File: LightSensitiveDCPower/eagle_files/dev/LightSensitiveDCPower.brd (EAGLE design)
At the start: 12 x 17.5 mm, 5 parts, among them SW1 PCM12SMTR

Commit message: Elongate board to save for wiidth. Check point.
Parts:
- moved OUT 4.47 mm to (6.00, 2.00), turned to 0 degrees
- moved PC1 4.03 mm to (6.00, 14.5)
- moved R1 4.03 mm to (5.50, 7.50)
- moved IN 3.92 mm to (5.00, 19.0)
- moved SW1 1.58 mm to (2.00, 12.5)
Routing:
- net N$1: track 21.2 -> 27.8 mm
- net N$2: track 2.68 -> 4.66 mm
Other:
- board size 12 x 17.5 mm -> 10 x 21 mm
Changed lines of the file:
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@@
 <layer number="37" name="tTest" color="7" fill="1" visible="no" active="yes"/>
 <layer number="38" name="bTest" color="7" fill="1" visible="no" active="yes"/>
-<layer number="39" name="tKeepout" color="4" fill="11" visible="no" active="yes"/>
+<layer number="39" name="tKeepout" color="4" fill="11" visible="yes" active="yes"/>
 <layer number="40" name="bKeepout" color="1" fill="11" visible="yes" active="yes"/>
 <layer number="41" name="tRestrict" color="4" fill="10" visible="yes" active="yes"/>
@@
 <board>
 <plain>
-<wire x1="0" y1="0" x2="12" y2="0" width="0" layer="20"/>
-<wire x1="12" y1="0" x2="12" y2="17.5" width="0" layer="20"/>
-<wire x1="12" y1="17.5" x2="0" y2="17.5" width="0" layer="20"/>
-<wire x1="0" y1="17.5" x2="0" y2="0" width="0" layer="20"/>
-<text x="2" y="15.25" size="0.6096" layer="51">VIN</text>
-<text x="1.25" y="0.5" size="0.6096" layer="51">VOUT</text>
-<text x="1.25" y="7" size="0.6096" layer="51">GND</text>
-<text x="10" y="15.25" size="0.6096" layer="51">GND</text>
-<text x="1.46" y="10.41" size="0.3048" layer="51">LiSePow
+<wire x1="0" y1="-0.01" x2="10" y2="0" width="0" layer="20"/>
+<wire x1="10" y1="0" x2="10" y2="21" width="0" layer="20"/>
+<wire x1="10" y1="21" x2="-0.01" y2="21" width="0" layer="20"/>
+<wire x1="-0.01" y1="21" x2="0" y2="-0.01" width="0" layer="20"/>
+<text x="0.7" y="18.5" size="0.6096" layer="51">VIN</text>
+<text x="9.49" y="0.88" size="0.6096" layer="51" rot="R90">VOUT</text>
+<text x="2.77" y="1.16" size="0.6096" layer="51" rot="R90">GND</text>
+<text x="8" y="18.5" size="0.6096" layer="51">GND</text>
+<text x="1.31" y="12.87" size="0.3048" layer="51">LiSePow
 Rev1
 09/19/14</text>
@@
 </autorouter>
 <elements>
-<element name="IN" library="pinhead" package="1X02" value="" x="6.67" y="15.45" smashed="yes" rot="R180">
-<attribute name="VALUE" x="9.21" y="18.625" size="1.27" layer="27" rot="R180"/>
-</element>
-<element name="OUT" library="pinhead" package="1X02" value="" x="2" y="4" smashed="yes" rot="R270">
-<attribute name="VALUE" x="-1.175" y="6.54" size="1.27" layer="27" rot="R270"/>
-</element>
-<element name="PC1" library="freddyLibr" package="PHOTOCELL_CERAMIC" value="" x="8" y="11" smashed="yes">
-<attribute name="NAME" x="3.48" y="12.67" size="0.8128" layer="25"/>
-</element>
-<element name="R1" library="pot" package="B25P" value="" x="7.5" y="4" smashed="yes">
-<attribute name="NAME" x="3.325" y="7.76" size="0.8128" layer="25" ratio="10"/>
-<attribute name="VALUE" x="4.3504" y="-1.08" size="1.27" layer="27" ratio="10"/>
-</element>
-<element name="SW1" library="freddyLibr" package="PCM12SMTR" value="PCM12SMTR" x="2.5" y="11" smashed="yes" rot="MR90">
-<attribute name="NAME" x="3.13" y="15.63" size="0.8128" layer="26" rot="MR0"/>
+<element name="IN" library="pinhead" package="1X02" value="" x="5" y="19" smashed="yes" rot="R180">
+<attribute name="VALUE" x="7.54" y="22.175" size="1.27" layer="27" rot="R180"/>
+</element>
+<element name="OUT" library="pinhead" package="1X02" value="" x="6" y="2" smashed="yes">
+<attribute name="VALUE" x="3.46" y="-1.175" size="1.27" layer="27"/>
+</element>
+<element name="PC1" library="freddyLibr" package="PHOTOCELL_CERAMIC" value="" x="6" y="14.5" smashed="yes">
+<attribute name="NAME" x="1.48" y="16.17" size="0.8128" layer="25"/>
+</element>
+<element name="R1" library="pot" package="B25P" value="" x="5.5" y="7.5" smashed="yes">
+<attribute name="NAME" x="1.325" y="11.26" size="0.8128" layer="25" ratio="10"/>
+<attribute name="VALUE" x="2.3504" y="2.42" size="1.27" layer="27" ratio="10"/>
+</element>
+<element name="SW1" library="freddyLibr" package="PCM12SMTR" value="PCM12SMTR" x="2" y="12.5" smashed="yes" rot="MR90">
+<attribute name="NAME" x="2.63" y="17.13" size="0.8128" layer="26" rot="MR0"/>
 </element>
 </elements>
@@
 <contactref element="R1" pad="A"/>
 <contactref element="OUT" pad="1"/>
-<wire x1="2" y1="5.27" x2="3.69" y2="5.27" width="0.4064" layer="1"/>
-<wire x1="3.69" y1="5.27" x2="4.96" y2="4" width="0.4064" layer="1"/>
-<wire x1="4.96" y1="4" x2="4.96" y2="8.04" width="0.4064" layer="16"/>
-<wire x1="4.96" y1="8.04" x2="4.25" y2="8.75" width="0.4064" layer="16"/>
-<wire x1="7.94" y1="15.45" x2="7.94" y2="14.48" width="0.4064" layer="1"/>
-<wire x1="7.94" y1="14.48" x2="4.96" y2="11.5" width="0.4064" layer="1"/>
-<wire x1="4.96" y1="11.5" x2="4.96" y2="4" width="0.4064" layer="1"/>
+<wire x1="2.96" y1="7.5" x2="2.96" y2="3.77" width="0.4064" layer="1"/>
+<wire x1="2.96" y1="3.77" x2="4.73" y2="2" width="0.4064" layer="1"/>
+<wire x1="4.73" y1="2" x2="4.73" y2="9.27" width="0.4064" layer="16"/>
+<wire x1="4.73" y1="9.27" x2="3.75" y2="10.25" width="0.4064" layer="16"/>
+<wire x1="6.27" y1="19" x2="6.27" y2="18.36" width="0.4064" layer="1"/>
+<wire x1="6.27" y1="18.36" x2="3.74" y2="15.83" width="0.4064" layer="1"/>
+<wire x1="3.74" y1="15.83" x2="3.74" y2="8.28" width="0.4064" layer="1"/>
+<wire x1="3.74" y1="8.28" x2="2.96" y2="7.5" width="0.4064" layer="1"/>
 </signal>
 <signal name="N$2">
 <contactref element="IN" pad="2"/>
 <contactref element="SW1" pad="3"/>
-<wire x1="5.4" y1="15.45" x2="5.4" y2="14.4" width="0.4064" layer="16"/>
-<wire x1="5.4" y1="14.4" x2="4.25" y2="13.25" width="0.4064" layer="16"/>
+<wire x1="3.73" y1="19" x2="3.73" y2="17.64" width="0.4064" layer="16"/>
+<wire x1="3.73" y1="17.64" x2="4.24" y2="17.13" width="0.4064" layer="16"/>
+<wire x1="4.24" y1="17.13" x2="4.24" y2="15.24" width="0.4064" layer="16"/>
+<wire x1="4.24" y1="15.24" x2="3.75" y2="14.75" width="0.4064" layer="16"/>
 </signal>
 <signal name="N$3">
 <contactref element="SW1" pad="2"/>
 <contactref element="PC1" pad="1"/>
-<wire x1="8" y1="12.7" x2="6.45" y2="12.7" width="0.4064" layer="16"/>
-<wire x1="6.45" y1="12.7" x2="5.5" y2="11.75" width="0.4064" layer="16"/>
-<wire x1="5.5" y1="11.75" x2="4.25" y2="11.75" width="0.4064" layer="16"/>
+<wire x1="6" y1="16.2" x2="6" y2="14.57" width="0.4064" layer="16"/>
+<wire x1="6" y1="14.57" x2="4.68" y2="13.25" width="0.4064" layer="16"/>
+<wire x1="4.68" y1="13.25" x2="3.75" y2="13.25" width="0.4064" layer="16"/>
 </signal>
 <signal name="N$4">
@@
 <contactref element="OUT" pad="2"/>
 <contactref element="PC1" pad="2"/>
-<wire x1="8" y1="9.3" x2="8" y2="7.04" width="0.4064" layer="1"/>
-<wire x1="8" y1="7.04" x2="7.5" y2="6.54" width="0.4064" layer="1"/>
-<wire x1="7.5" y1="6.54" x2="7.5" y2="4.23" width="0.4064" layer="1"/>
-<wire x1="7.5" y1="4.23" x2="6" y2="2.73" width="0.4064" layer="1"/>
-<wire x1="6" y1="2.73" x2="2" y2="2.73" width="0.4064" layer="1"/>
+<wire x1="5.5" y1="10.04" x2="5.5" y2="12.3" width="0.4064" layer="1"/>
+<wire x1="5.5" y1="12.3" x2="6" y2="12.8" width="0.4064" layer="1"/>
+<wire x1="5.5" y1="10.04" x2="5.5" y2="3.77" width="0.4064" layer="1"/>
+<wire x1="5.5" y1="3.77" x2="7.27" y2="2" width="0.4064" layer="1"/>
 </signal>
 </signals>

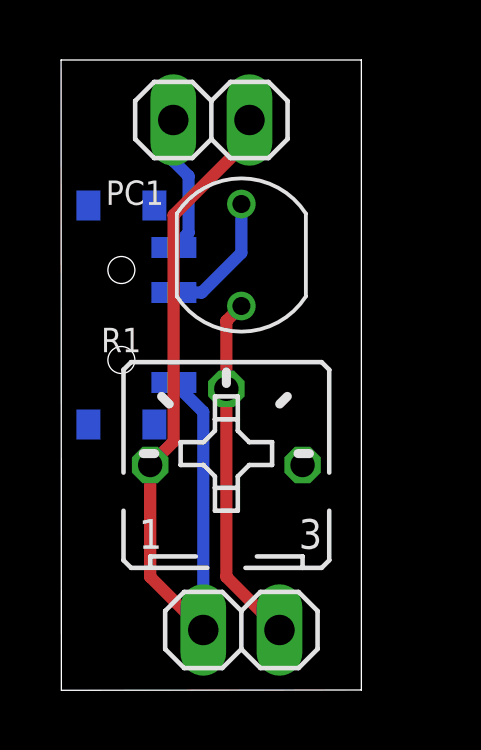
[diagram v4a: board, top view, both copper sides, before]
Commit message: Slightly tweaked parts for a narrower board and production files.
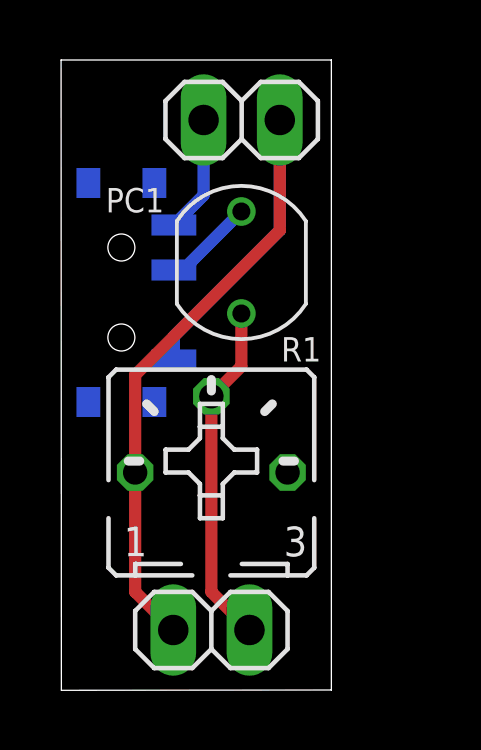
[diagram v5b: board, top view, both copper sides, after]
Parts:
- moved IN 1.01 mm to (6.01, 19.0)
- moved OUT 1.00 mm to (5.00, 2.00)
- moved SW1 0.75 mm to (2.00, 13.2)
- moved R1 0.56 mm to (5.00, 7.25)
- moved PC1 0.25 mm to (6.00, 14.2)
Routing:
- net N$3: track 4.43 -> 3.06 mm
- net N$1: track 27.8 -> 29.0 mm
- net N$2: track 4.66 -> 3.91 mm
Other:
- board size 10 x 21 mm -> 9 x 21 mm
- board text added: "LiSePow Rev1 09/27/14"
- board text removed: "LiSePow Rev1 09/19/14"
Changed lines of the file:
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@@
 <board>
 <plain>
-<wire x1="0" y1="-0.01" x2="10" y2="0" width="0" layer="20"/>
-<wire x1="10" y1="0" x2="10" y2="21" width="0" layer="20"/>
-<wire x1="10" y1="21" x2="-0.01" y2="21" width="0" layer="20"/>
+<wire x1="0" y1="-0.01" x2="9" y2="0" width="0" layer="20"/>
+<wire x1="9" y1="0" x2="9" y2="21" width="0" layer="20"/>
+<wire x1="9" y1="21" x2="-0.01" y2="21" width="0" layer="20"/>
 <wire x1="-0.01" y1="21" x2="0" y2="-0.01" width="0" layer="20"/>
-<text x="0.7" y="18.5" size="0.6096" layer="51">VIN</text>
-<text x="9.49" y="0.88" size="0.6096" layer="51" rot="R90">VOUT</text>
-<text x="2.77" y="1.16" size="0.6096" layer="51" rot="R90">GND</text>
-<text x="8" y="18.5" size="0.6096" layer="51">GND</text>
-<text x="1.31" y="12.87" size="0.3048" layer="51">LiSePow
+<text x="2" y="19.94" size="0.6096" layer="51">VIN</text>
+<text x="8.49" y="0.88" size="0.6096" layer="51" rot="R90">VOUT</text>
+<text x="2.07" y="1.08" size="0.6096" layer="51" rot="R90">GND</text>
+<text x="7.08" y="16.74" size="0.6096" layer="51">GND</text>
+<text x="1.09" y="12.62" size="0.3048" layer="51">LiSePow
 Rev1
-09/19/14</text>
+09/27/14</text>
 </plain>
 <attributes>
@@
 </autorouter>
 <elements>
-<element name="IN" library="pinhead" package="1X02" value="" x="5" y="19" smashed="yes" rot="R180">
-<attribute name="VALUE" x="7.54" y="22.175" size="1.27" layer="27" rot="R180"/>
-</element>
-<element name="OUT" library="pinhead" package="1X02" value="" x="6" y="2" smashed="yes">
-<attribute name="VALUE" x="3.46" y="-1.175" size="1.27" layer="27"/>
-</element>
-<element name="PC1" library="freddyLibr" package="PHOTOCELL_CERAMIC" value="" x="6" y="14.5" smashed="yes">
-<attribute name="NAME" x="1.48" y="16.17" size="0.8128" layer="25"/>
-</element>
-<element name="R1" library="pot" package="B25P" value="" x="5.5" y="7.5" smashed="yes">
-<attribute name="NAME" x="1.325" y="11.26" size="0.8128" layer="25" ratio="10"/>
-<attribute name="VALUE" x="2.3504" y="2.42" size="1.27" layer="27" ratio="10"/>
-</element>
-<element name="SW1" library="freddyLibr" package="PCM12SMTR" value="PCM12SMTR" x="2" y="12.5" smashed="yes" rot="MR90">
-<attribute name="NAME" x="2.63" y="17.13" size="0.8128" layer="26" rot="MR0"/>
+<element name="IN" library="pinhead" package="1X02" value="" x="6.01" y="19" smashed="yes" rot="R180">
+<attribute name="VALUE" x="8.55" y="22.175" size="1.27" layer="27" rot="R180"/>
+</element>
+<element name="OUT" library="pinhead" package="1X02" value="" x="5" y="2" smashed="yes">
+<attribute name="VALUE" x="2.46" y="-1.175" size="1.27" layer="27"/>
+</element>
+<element name="PC1" library="freddyLibr" package="PHOTOCELL_CERAMIC" value="" x="6" y="14.25" smashed="yes">
+<attribute name="NAME" x="1.48" y="15.92" size="0.8128" layer="25"/>
+</element>
+<element name="R1" library="pot" package="B25P" value="" x="5" y="7.25" smashed="yes">
+<attribute name="NAME" x="7.325" y="10.95" size="0.8128" layer="25" ratio="10"/>
+<attribute name="VALUE" x="1.8504" y="2.17" size="1.27" layer="27" ratio="10"/>
+</element>
+<element name="SW1" library="freddyLibr" package="PCM12SMTR" value="PCM12SMTR" x="2" y="13.25" smashed="yes" rot="MR90">
+<attribute name="NAME" x="2.63" y="17.88" size="0.8128" layer="26" rot="MR0"/>
 </element>
 </elements>
@@
 <contactref element="R1" pad="A"/>
 <contactref element="OUT" pad="1"/>
-<wire x1="2.96" y1="7.5" x2="2.96" y2="3.77" width="0.4064" layer="1"/>
-<wire x1="2.96" y1="3.77" x2="4.73" y2="2" width="0.4064" layer="1"/>
-<wire x1="4.73" y1="2" x2="4.73" y2="9.27" width="0.4064" layer="16"/>
-<wire x1="4.73" y1="9.27" x2="3.75" y2="10.25" width="0.4064" layer="16"/>
-<wire x1="6.27" y1="19" x2="6.27" y2="18.36" width="0.4064" layer="1"/>
-<wire x1="6.27" y1="18.36" x2="3.74" y2="15.83" width="0.4064" layer="1"/>
-<wire x1="3.74" y1="15.83" x2="3.74" y2="8.28" width="0.4064" layer="1"/>
-<wire x1="3.74" y1="8.28" x2="2.96" y2="7.5" width="0.4064" layer="1"/>
+<wire x1="2.46" y1="7.25" x2="2.46" y2="3.27" width="0.4064" layer="1"/>
+<wire x1="2.46" y1="3.27" x2="3.73" y2="2" width="0.4064" layer="1"/>
+<wire x1="7.28" y1="19" x2="7.28" y2="15.32" width="0.4064" layer="1"/>
+<wire x1="7.28" y1="15.32" x2="2.46" y2="10.5" width="0.4064" layer="1"/>
+<wire x1="2.46" y1="10.5" x2="2.46" y2="7.25" width="0.4064" layer="1"/>
+<wire x1="3.75" y1="11" x2="3.75" y2="11.79" width="0.4064" layer="16"/>
+<wire x1="3.75" y1="11.79" x2="7.28" y2="15.32" width="0.4064" layer="16"/>
+<wire x1="7.28" y1="15.32" x2="7.28" y2="19" width="0.4064" layer="16"/>
 </signal>
 <signal name="N$2">
 <contactref element="IN" pad="2"/>
 <contactref element="SW1" pad="3"/>
-<wire x1="3.73" y1="19" x2="3.73" y2="17.64" width="0.4064" layer="16"/>
-<wire x1="3.73" y1="17.64" x2="4.24" y2="17.13" width="0.4064" layer="16"/>
-<wire x1="4.24" y1="17.13" x2="4.24" y2="15.24" width="0.4064" layer="16"/>
-<wire x1="4.24" y1="15.24" x2="3.75" y2="14.75" width="0.4064" layer="16"/>
+<wire x1="4.74" y1="19" x2="4.74" y2="16.49" width="0.4064" layer="16"/>
+<wire x1="4.74" y1="16.49" x2="3.75" y2="15.5" width="0.4064" layer="16"/>
 </signal>
 <signal name="N$3">
 <contactref element="SW1" pad="2"/>
 <contactref element="PC1" pad="1"/>
-<wire x1="6" y1="16.2" x2="6" y2="14.57" width="0.4064" layer="16"/>
-<wire x1="6" y1="14.57" x2="4.68" y2="13.25" width="0.4064" layer="16"/>
-<wire x1="4.68" y1="13.25" x2="3.75" y2="13.25" width="0.4064" layer="16"/>
+<wire x1="3.75" y1="14" x2="4.05" y2="14" width="0.4064" layer="16"/>
+<wire x1="4.05" y1="14" x2="6" y2="15.95" width="0.4064" layer="16"/>
 </signal>
 <signal name="N$4">
@@
 <contactref element="OUT" pad="2"/>
 <contactref element="PC1" pad="2"/>
-<wire x1="5.5" y1="10.04" x2="5.5" y2="12.3" width="0.4064" layer="1"/>
-<wire x1="5.5" y1="12.3" x2="6" y2="12.8" width="0.4064" layer="1"/>
-<wire x1="5.5" y1="10.04" x2="5.5" y2="3.77" width="0.4064" layer="1"/>
-<wire x1="5.5" y1="3.77" x2="7.27" y2="2" width="0.4064" layer="1"/>
+<wire x1="6" y1="12.55" x2="6" y2="10.79" width="0.4064" layer="1"/>
+<wire x1="6" y1="10.79" x2="5" y2="9.79" width="0.4064" layer="1"/>
+<wire x1="5" y1="9.79" x2="5" y2="3.27" width="0.4064" layer="1"/>
+<wire x1="5" y1="3.27" x2="6.27" y2="2" width="0.4064" layer="1"/>
 </signal>
 </signals>
